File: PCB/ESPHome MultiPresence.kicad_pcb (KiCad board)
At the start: 2 copper layers, 33 parts, among them J1 Conn_01x06, J2 USB_C_Receptacle_Power, J3 Conn_01x02, J4 Conn_01x03, SW1 SW_Push, SW2 SW_Push, U1 ESP32-WROOM-32, U2 SEN0395, U3 EKMC1603113, U4 TSL2591, U5 SHTC3, U6 TLV75533PDBV

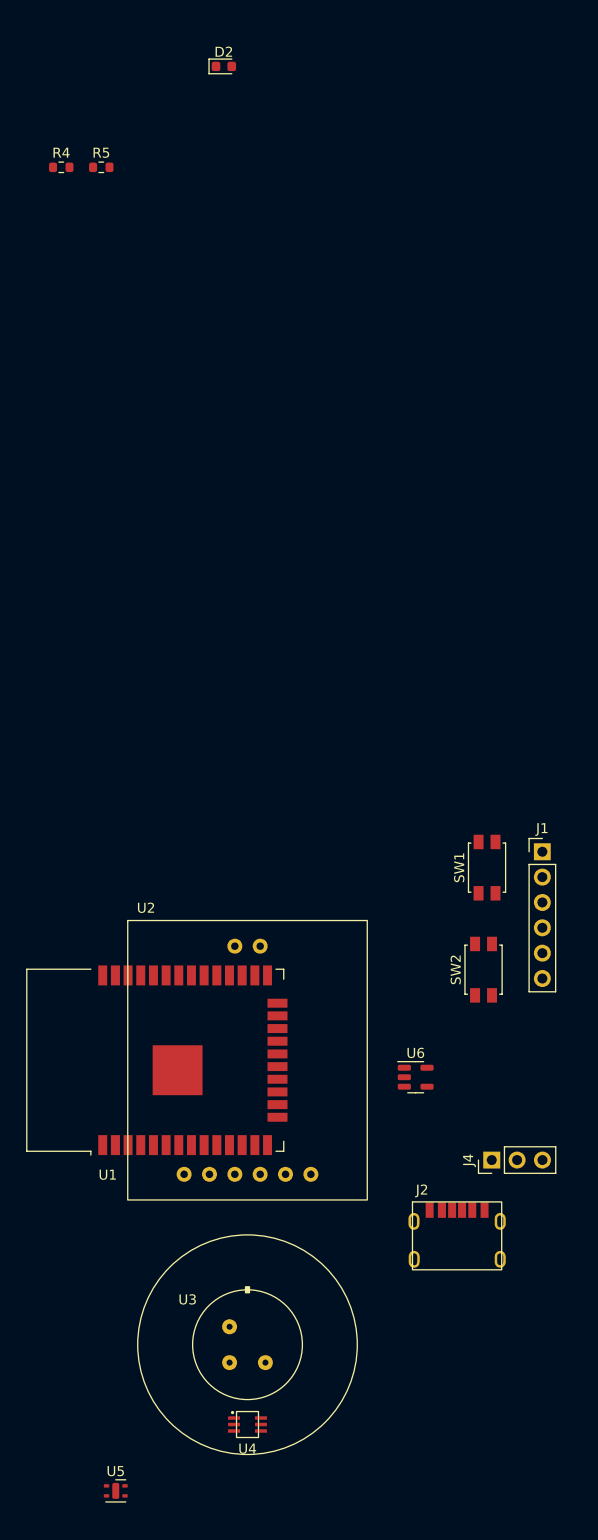
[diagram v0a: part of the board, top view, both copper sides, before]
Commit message: Moved kicad files to the PCB folder
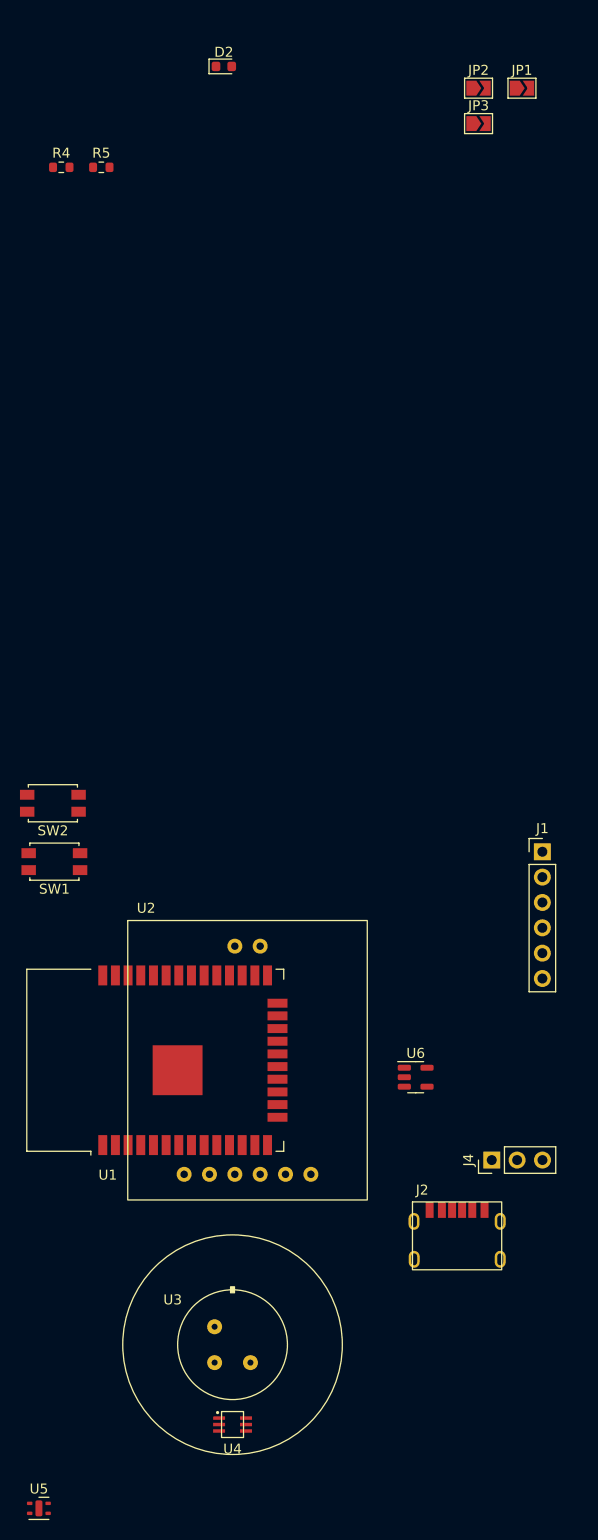
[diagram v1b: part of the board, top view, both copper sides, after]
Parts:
- added JP1: OpenJumper, Jumper:SolderJumper-2_P1.3mm_Open_TrianglePad1.0x1.5mm, F.Cu at (179.0, -21.9)
- added JP2: OpenJumper, Jumper:SolderJumper-2_P1.3mm_Open_TrianglePad1.0x1.5mm, F.Cu at (174.7, -21.9)
- added JP3: OpenJumper, Jumper:SolderJumper-2_P1.3mm_Open_TrianglePad1.0x1.5mm, F.Cu at (174.7, -18.4)
- moved SW2 46.3 mm to (132.0, 49.8), turned to 180 degrees
- moved SW1 43.4 mm to (132.2, 55.6), turned to 180 degrees
- moved U5 7.90 mm to (130.6, 120.4)
- moved U3 1.50 mm to (150.0, 104.0)
- moved U4 1.50 mm to (150.0, 112.0)
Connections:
- R2 pad 1: +3.3V -> Net-(R2-Pad1)
- R3 pad 1: +5V -> Net-(R3-Pad1)
- R9 pad 1: LED_BUILTIN -> Net-(R9-Pad1)

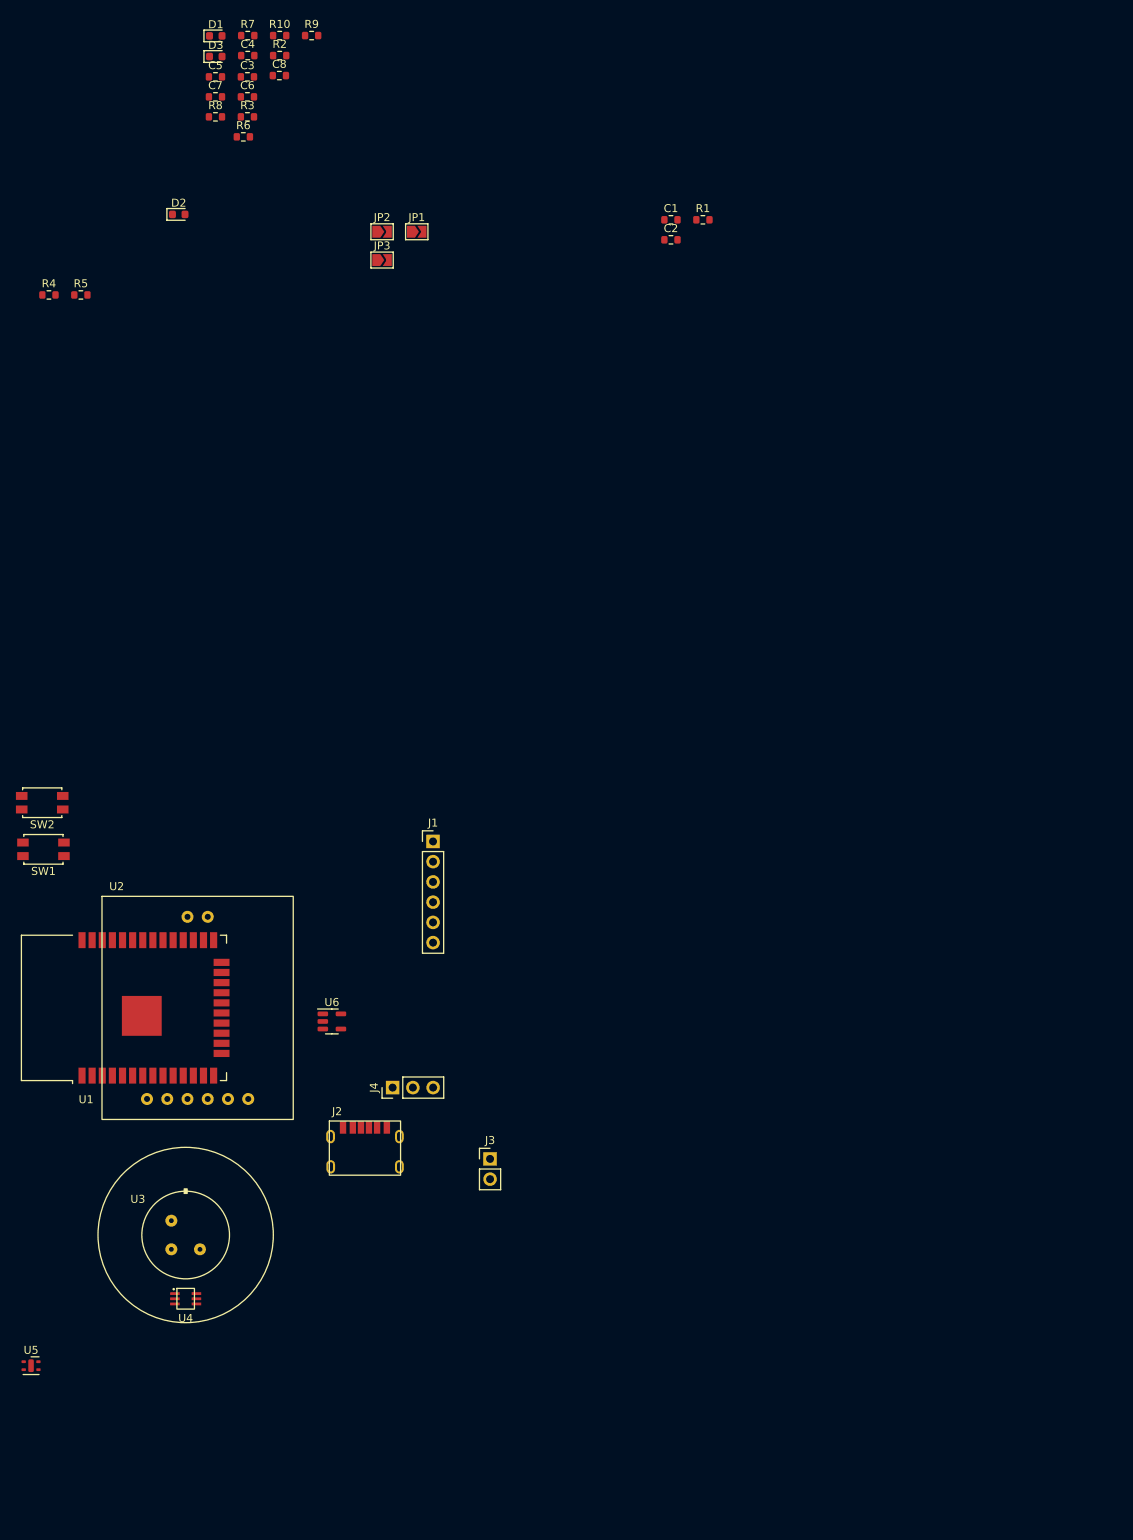
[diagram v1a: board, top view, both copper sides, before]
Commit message: updated footprints and started board layout
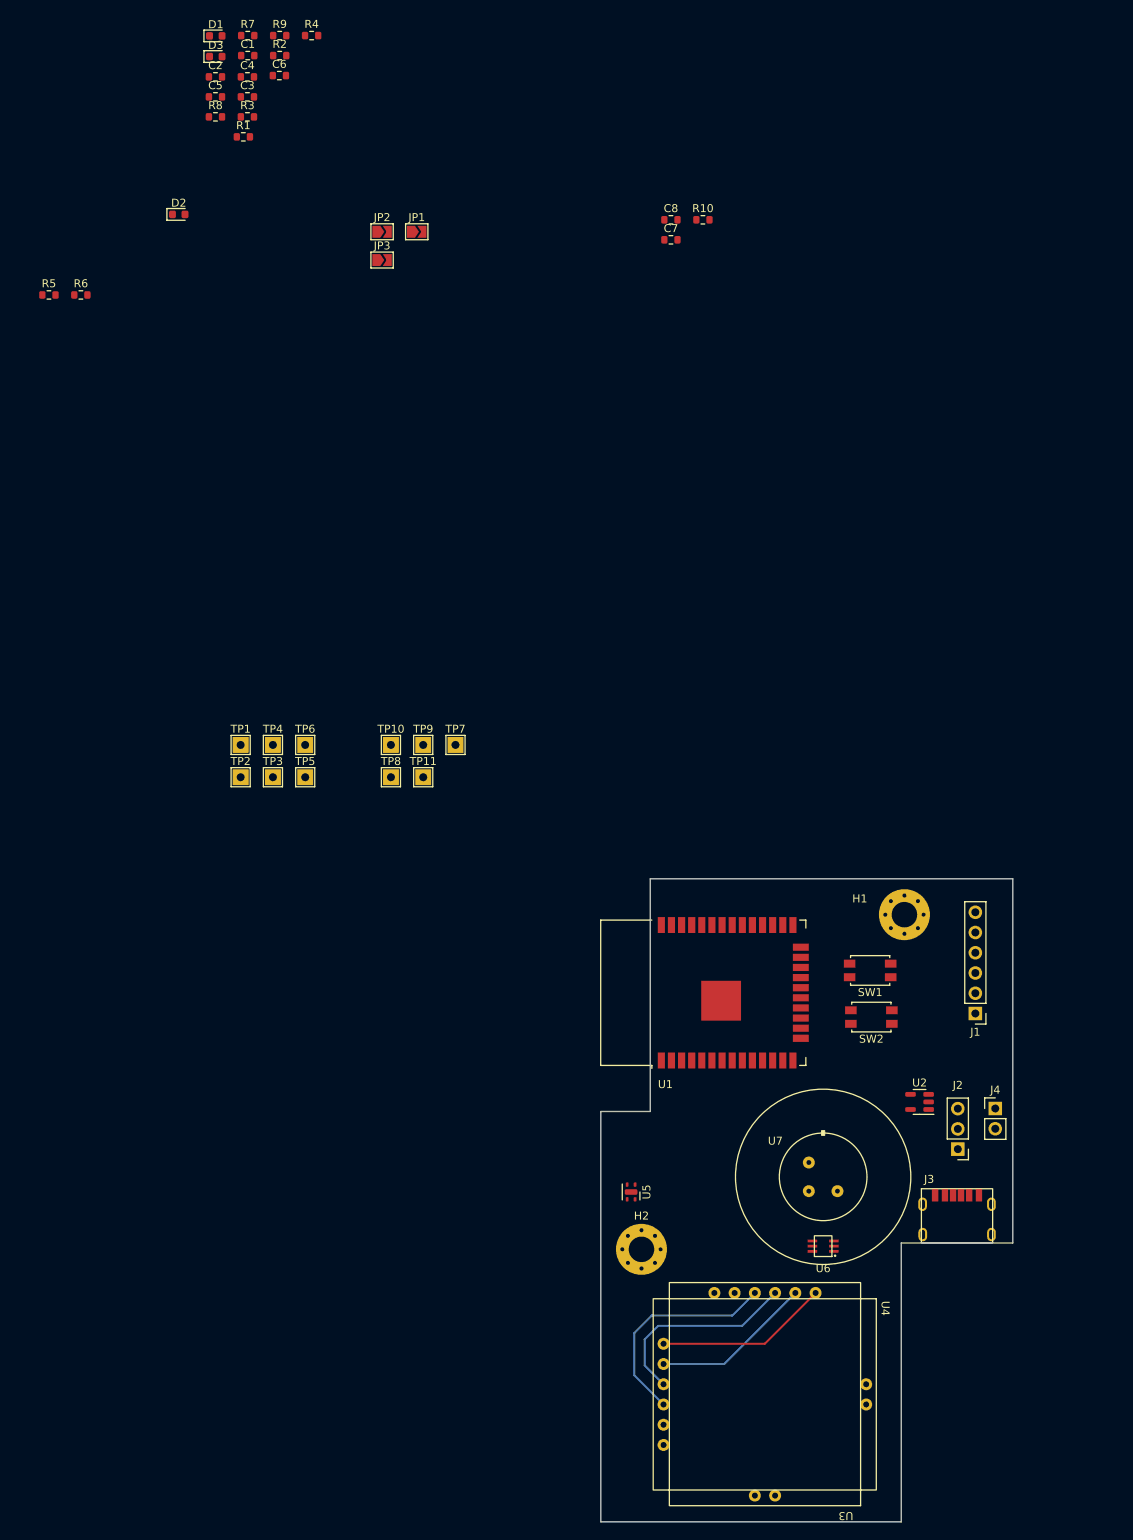
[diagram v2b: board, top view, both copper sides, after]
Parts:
- added H1: MountingHole, MountingHole:MountingHole_3.2mm_M3_Pad_Via, F.Cu at (240.2, 63.8)
- added H2: MountingHole, MountingHole:MountingHole_3.2mm_M3_Pad_Via, F.Cu at (207.2, 105.8)
- added TP1: TestPoint, TestPoint:TestPoint_THTPad_2.0x2.0mm_Drill1.0mm, F.Cu at (156.9, 42.5)
- added TP10: TestPoint, TestPoint:TestPoint_THTPad_2.0x2.0mm_Drill1.0mm, F.Cu at (175.8, 42.5)
- added TP11: TestPoint, TestPoint:TestPoint_THTPad_2.0x2.0mm_Drill1.0mm, F.Cu at (179.8, 46.5)
- added TP2: TestPoint, TestPoint:TestPoint_THTPad_2.0x2.0mm_Drill1.0mm, F.Cu at (156.9, 46.5)
- added TP3: TestPoint, TestPoint:TestPoint_THTPad_2.0x2.0mm_Drill1.0mm, F.Cu at (160.9, 46.5)
- added TP4: TestPoint, TestPoint:TestPoint_THTPad_2.0x2.0mm_Drill1.0mm, F.Cu at (160.9, 42.5)
- added TP5: TestPoint, TestPoint:TestPoint_THTPad_2.0x2.0mm_Drill1.0mm, F.Cu at (165.0, 46.5)
- added TP6: TestPoint, TestPoint:TestPoint_THTPad_2.0x2.0mm_Drill1.0mm, F.Cu at (165.0, 42.5)
- added TP7: TestPoint, TestPoint:TestPoint_THTPad_2.0x2.0mm_Drill1.0mm, F.Cu at (183.9, 42.5)
- added TP8: TestPoint, TestPoint:TestPoint_THTPad_2.0x2.0mm_Drill1.0mm, F.Cu at (175.8, 46.5)
- added TP9: TestPoint, TestPoint:TestPoint_THTPad_2.0x2.0mm_Drill1.0mm, F.Cu at (179.8, 42.5)
- added U4: SEN0395, My Footprints:SEN0395, F.Cu at (222.7, 124.0)
- moved SW1 106.0 mm to (235.9, 70.8)
- moved SW2 106.0 mm to (236.1, 76.7)
- moved U3 86.1 mm to (222.7, 124.0), turned to 180 degrees
- moved U7 80.3 mm to (230.0, 96.7)
- moved U6 80.3 mm to (230.0, 105.4), turned to 180 degrees
- moved U5 78.4 mm to (205.9, 98.6), turned to -90 degrees
- moved J3 74.8 mm to (246.8, 98.2)
- moved U2 74.4 mm to (242.1, 87.3), turned to 180 degrees
- moved U1 72.7 mm to (217.9, 73.6)
- moved J1 71.4 mm to (249.1, 76.2), turned to 180 degrees
- moved J2 71.3 mm to (246.9, 93.2), turned to 180 degrees
- moved J4 63.7 mm to (251.6, 88.1)
- renumbered C4 to C1, C5 to C2, C6 to C3, C3 to C4, C7 to C5, C8 to C6, C2 to C7, C1 to C8, J4 to J2, J2 to J3, J3 to J4, R6 to R1, R1 to R10, R9 to R4, R4 to R5, R5 to R6, R10 to R9, SW2 to SW1, SW1 to SW2, U6 to U2, U2 to U3, U4 to U6, U3 to U7
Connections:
- U1 pad 13: unconnected-(U1-Pad13) -> RADAR_TX
- U1 pad 16: unconnected-(U1-Pad16) -> RADAR_RX
- U1 pad 23: unconnected-(U1-Pad23) -> RADAR_GPIO1
- U1 pad 27: unconnected-(U1-Pad27) -> PRESENCE
- U3 pad 3: unconnected-(U2-Pad3) -> RADAR_GPIO1
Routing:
- net PRESENCE: track 0.00 -> 27.7 mm
- net RADAR_GPIO1: track 0.00 -> 25.4 mm
- net RADAR_TX: track 0.00 -> 21.7 mm
- net RADAR_RX: track 0.00 -> 20.2 mm
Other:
- board outline added: 51.7 x 80.7 mm

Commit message: board layout work
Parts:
- removed the TP5 at (165.0, 46.5)
- removed the TP6 at (165.0, 42.5)
- moved R9 168.5 mm to (250.7, 96.6)
- moved C2 166.3 mm to (258.6, 87.7), turned to -90 degrees
- moved C6 164.8 mm to (265.7, 86.4)
- moved C1 164.8 mm to (261.7, 83.9)
- moved R8 163.2 mm to (250.7, 95.0)
- moved R7 154.2 mm to (215.4, 96.5), turned to -90 degrees
- moved C5 153.0 mm to (244.1, 84.6)
- moved C4 147.2 mm to (242.6, 79.0)
- moved D3 140.1 mm to (187.1, 92.2), turned to 180 degrees
- moved R4 139.8 mm to (183.1, 92.2)
- moved C3 139.6 mm to (241.3, 73.0)
- moved R5 137.0 mm to (232.0, 80.6)
- moved D1 135.0 mm to (187.1, 84.4), turned to 180 degrees
- moved R6 133.9 mm to (212.7, 96.4)
- moved R2 130.2 mm to (183.1, 84.4)
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- renumbered TP7 to TP5, TP8 to TP6, TP9 to TP7, TP10 to TP8, TP11 to TP9, U5 to U4, U4 to U5
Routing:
- net +5V: track 0.00 -> 64.6 mm
- net Net-(J1-Pad5): track 0.00 -> 42.3 mm
- net Net-(J1-Pad4): track 0.00 -> 40.0 mm
- net Net-(J2-Pad1): track 0.00 -> 12.5 mm
- net Net-(J3-PadB5): track 0.00 -> 5.99 mm
- net Net-(J2-Pad3): track 0.00 -> 5.75 mm
- net Net-(J3-PadA5): track 0.00 -> 4.21 mm
